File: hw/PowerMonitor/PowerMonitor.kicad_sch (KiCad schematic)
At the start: 43 parts, among them J1 Conn_01x02_Socket, J2 Conn_01x02_Socket, J3 Conn_01x02_Socket, J4 Conn_01x02_Socket, J5 Conn_01x02_Socket, K1 Relay_SPST-NC, U1 TPS54202DDC, U2 74LVC1G32, U3 74LVC1G32, U4 NE555D

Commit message: Rework powermon
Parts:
- removed C1: 10 µF, Capacitor_SMD:C_0603_1608Metric_Pad1.08x0.95mm_HandSolder, symbol #inventree:CL21A106KOQNNNE
- removed C2, C3: 0.1 µF, Capacitor_SMD:C_0603_1608Metric_Pad1.08x0.95mm_HandSolder, symbol #inventree:CL21B104KBCNNNC
- removed C5, C6: 22 µF, Capacitor_SMD:C_0603_1608Metric_Pad1.08x0.95mm_HandSolder, symbol #inventree:CL21X226MOYNNWE
- removed D1: PESD15VL1BA, Diode_SMD:D_SOD-323_HandSoldering, symbol Device:D_TVS
- removed JP1: SolderJumper_2_Open, Jumper:SolderJumper-2_P1.3mm_Open_RoundedPad1.0x1.5mm, symbol Jumper:SolderJumper_2_Open
- removed L1: L_Ferrite_Coupled_1423, Inductor_SMD:L_CommonModeChoke_TDK_ACM7060, symbol Device:L_Ferrite_Coupled_1423
- removed L2: KOHER_MDA7030 15uH, Inductor_SMD:L_KOHERelec_MDA7030, symbol Device:L_Ferrite
- removed R1: 0 ohm, Resistor_SMD:R_0603_1608Metric_Pad0.98x0.95mm_HandSolder, symbol #inventree:RC0603FR-070RL
- removed R2: 100 kohm, Resistor_SMD:R_0603_1608Metric_Pad0.98x0.95mm_HandSolder, symbol #inventree:RC0603FR-07100KL
- removed R3: 22 kohm, Resistor_SMD:R_0603_1608Metric_Pad0.98x0.95mm_HandSolder, symbol #inventree:RC0603FR-0722KL
- removed TP1, TP2, TP3, TP4: TestPoint_Flag, TestPoint:TestPoint_Pad_1.0x1.0mm, symbol Connector:TestPoint_Flag
- removed U1: TPS54202DDC, Package_TO_SOT_SMD:SOT-23-6_Handsoldering, symbol Regulator_Switching:TPS54202DDC
- removed U2, U3: 74LVC1G32, Package_TO_SOT_SMD:SOT-353_SC-70-5_Handsoldering, symbol 74xGxx:74LVC1G32
- added C10: 470u, Capacitor_THT:CP_Radial_D4.0mm_P1.50mm, symbol Device:C_Polarized
- added C11: 1u, Capacitor_SMD:C_0603_1608Metric_Pad1.08x0.95mm_HandSolder, symbol Device:C
- added D5: PESD15VL1BA, Diode_SMD:D_SOD-323_HandSoldering, symbol Device:D_TVS
- added JP2: SolderJumper_2_Open, Jumper:SolderJumper-2_P1.3mm_Open_RoundedPad1.0x1.5mm, symbol Jumper:SolderJumper_2_Open
- added L3: L_Ferrite_Coupled_1423, Inductor_SMD:L_CommonModeChoke_TDK_ACM7060, symbol Device:L_Ferrite_Coupled_1423
- added R1: 50k, Resistor_SMD:R_0603_1608Metric_Pad0.98x0.95mm_HandSolder, symbol Device:R
- C4, C7: value 1u -> 100n
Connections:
- net +10V: now also C7.2, C8.1, U4.8 (VCC), C10.1, C11.2, D5.2 (A2)
- net +3V3: no longer C4.1, C7.1, C8.1, U4.8 (VCC)
- net GND: now also BT3.2 (-), C4.1, C7.1, C8.2, C10.2, C11.1, D5.1 (A1), R1.2
- net GNDREF: no longer BT3.2 (-), C4.2, C7.2, C8.2
- net CellMonitor1/UVOV: now reaches U4.2 (TR)
- net CellMonitor1/UVOV: now also C4.2, R1.1
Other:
- sheet CellMonitor1 ports: added UVOV; removed UVLO
- sheet CellMonitor2 ports: added UVOV; removed UVLO
- sheet CellMonitor3 ports: added UVOV; removed UVLO
- moved on the sheet: BT1, BT2, BT3, C22, C8, C9, D8, D9, J1, J2, J3, J4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

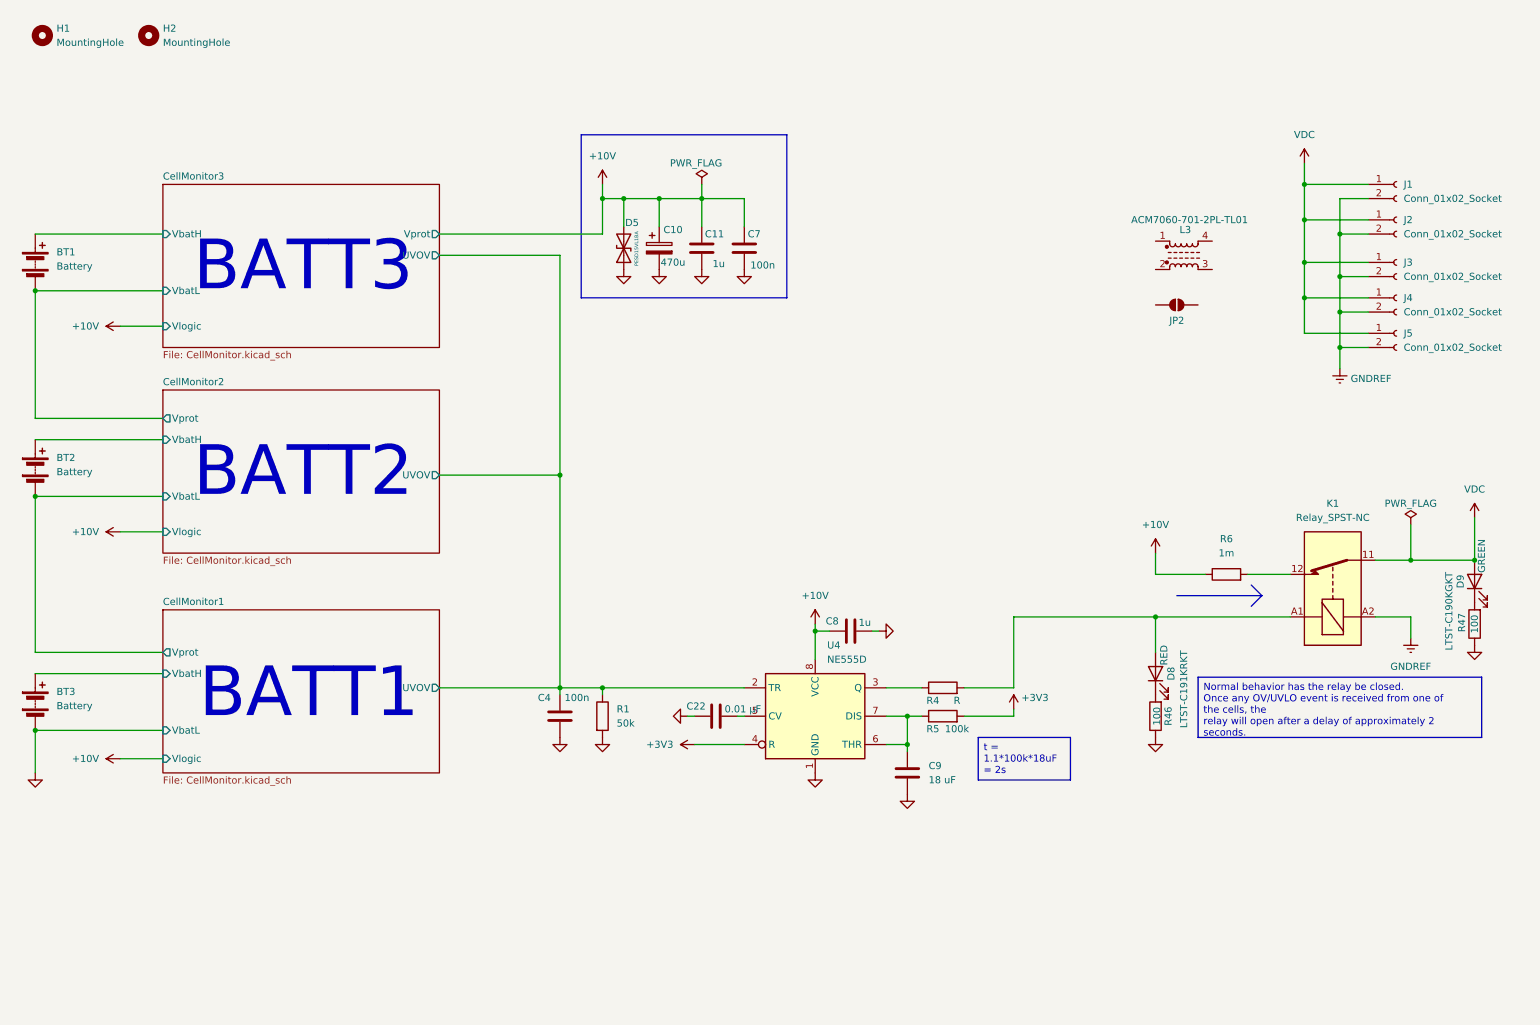
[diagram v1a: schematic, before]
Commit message: ad uvov in powermon, overcurrent and prepare for latch alarm
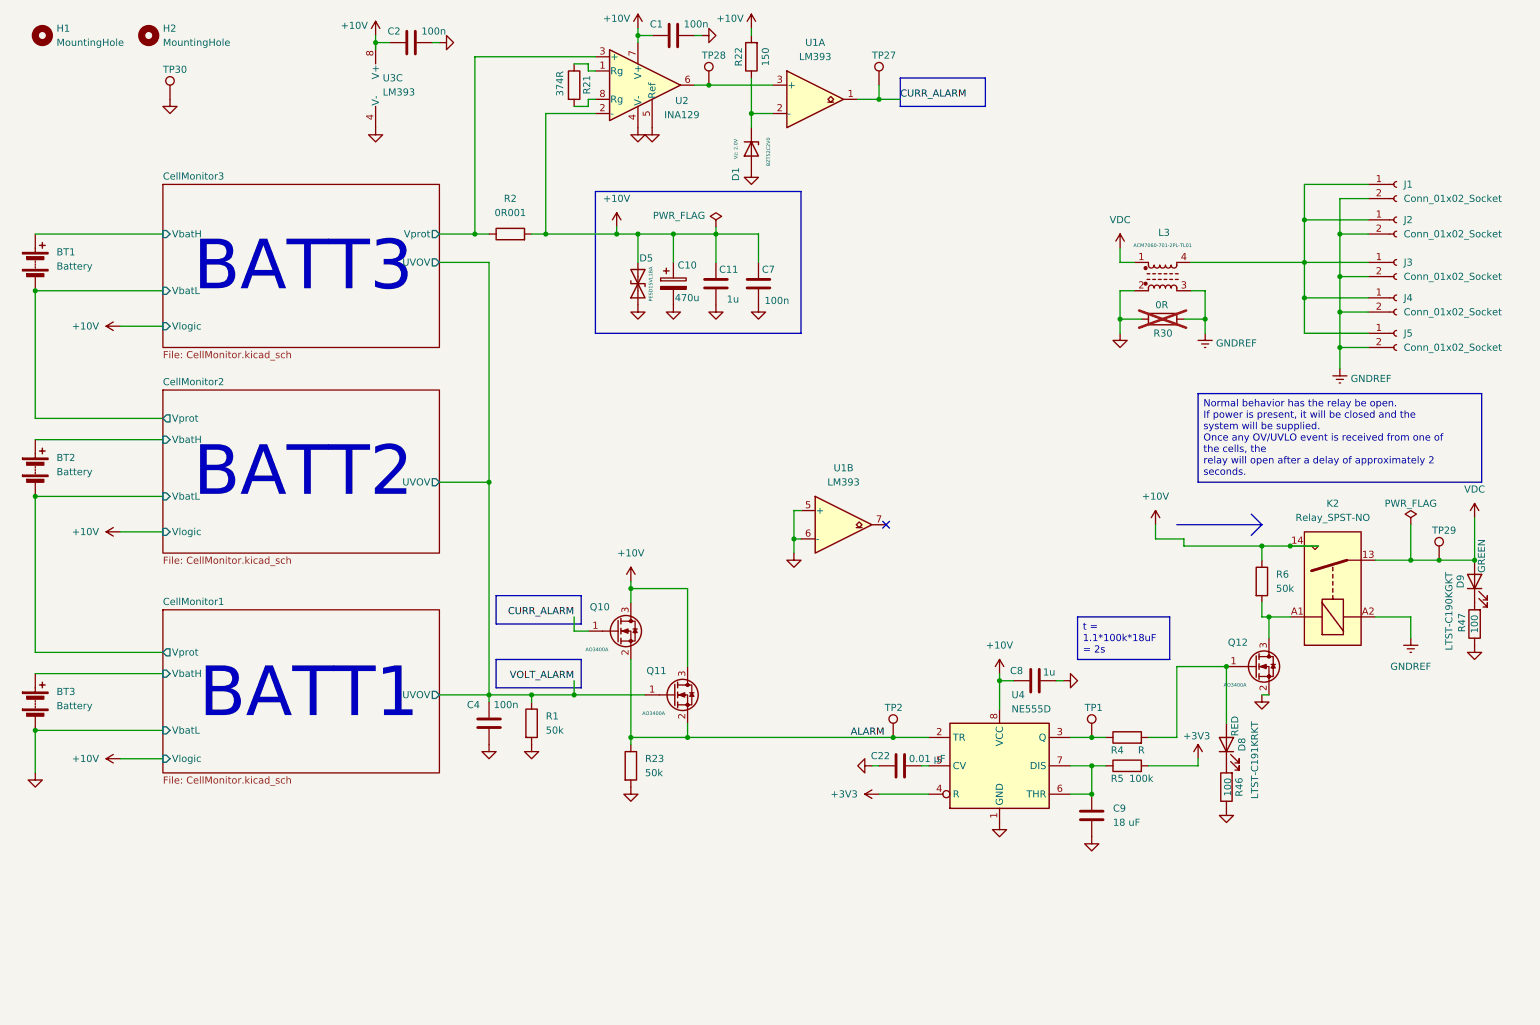
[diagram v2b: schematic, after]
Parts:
- removed JP2: SolderJumper_2_Open, Jumper:SolderJumper-2_P1.3mm_Open_RoundedPad1.0x1.5mm, symbol Jumper:SolderJumper_2_Open
- removed K1: Relay_SPST-NC, symbol Relay:Relay_SPST-NC
- added C1, C2: 100n, Capacitor_SMD:C_0603_1608Metric_Pad1.08x0.95mm_HandSolder, symbol Device:C
- added D1: BZT52Bxx, Diode_SMD:D_SOD-123F, symbol Diode:BZT52Bxx
- added K2: Relay_SPST-NO, symbol Relay:Relay_SPST-NO
- added Q10, Q11, Q12: AO3400A, Package_TO_SOT_SMD:SOT-23_Handsoldering, symbol Transistor_FET:AO3400A
- added R2: 0R001, Resistor_SMD:R_2512_6332Metric_Pad1.40x3.35mm_HandSolder, symbol Device:R
- added R21: 374R, Resistor_SMD:R_0603_1608Metric_Pad0.98x0.95mm_HandSolder, symbol Device:R
- added R22: 150, Resistor_SMD:R_0603_1608Metric_Pad0.98x0.95mm_HandSolder, symbol Device:R
- added R23: 50k, Resistor_SMD:R_0603_1608Metric_Pad0.98x0.95mm_HandSolder, symbol Device:R
- added R30: 0R, Resistor_SMD:R_0603_1608Metric_Pad0.98x0.95mm_HandSolder, symbol Device:R
- added TP1, TP2, TP27, TP28, TP29, TP30: TestPoint, Connector_Pin:Pin_D1.4mm_L8.5mm_W2.8mm_FlatFork, symbol Connector:TestPoint
- added U1, U3: LM393, Package_SO:SOIC-8_3.9x4.9mm_P1.27mm, symbol Comparator:LM393
- added U2: INA129, Package_SO:SOIC-8_5.3x6.2mm_P1.27mm, symbol Amplifier_Instrumentation:INA129
- R6: value 1m -> 50k; footprint Resistor_SMD:R_2512_6332Metric_Pad1.40x3.35mm_HandSolder -> Resistor_SMD:R_0603_1608Metric_Pad0.98x0.95mm_HandSolder
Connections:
- net +10V: now also C1.2, C2.2, K2.14, Q10.3 (D), Q11.3 (D), R2.2, R22.2, U2.2 (-), U2.7 (V+), U3.8 (V+)
- net GND: now also L3.2, C1.1, C2.1, D1.2 (A), Q12.2 (S), R23.2, R30.2, TP30.1, U1.5 (+), U1.6 (-), U2.4 (V-), U2.5 (Ref), U3.4 (V-)
- net GNDREF: now also L3.3, K2.A2, R30.1
- net VDC: now also L3.1, K2.13, TP29.1; no longer J1.1 (Pin_1), J2.1 (Pin_1), J3.1 (Pin_1), J4.1 (Pin_1), J5.1 (Pin_1)
- net at R4.1, U4.3 (Q): now also TP1.1
- net at D8.2 (A), R4.2: now also Q12.1 (G)
- net at R6.2: now also K2.A1, Q12.3 (D)
- net at L3.4: now also J1.1 (Pin_1), J2.1 (Pin_1), J3.1 (Pin_1), J4.1 (Pin_1), J5.1 (Pin_1)
- net CellMonitor1/UVOV renamed VOLT_ALARM
- net VOLT_ALARM: now also Q11.1 (G); no longer U4.2 (TR)
- new net: R21.1, U2.1 (Rg)
- new net: R21.2, U2.8 (Rg)
- new net: D1.1 (K), R22.1, U1.2 (-)
- new net: TP28.1, U1.3 (+), U2.6
- new net ALARM: Q10.2 (S), Q11.2 (S), R23.1, TP2.1, U4.2 (TR)
- new net CURR_ALARM: Q10.1 (G), TP27.1, U1.1
- new net CellMonitor3/Vprot: R2.1, U2.3 (+)
- no-connect marks 0 -> 1
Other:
- moved on the sheet: C10, C11, C22, C4, C7, C8, C9, D5, D8, L3, R1, R4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

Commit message: * hw/PowerMonitor/CellMonitor.kicad_sch: start PCB layout
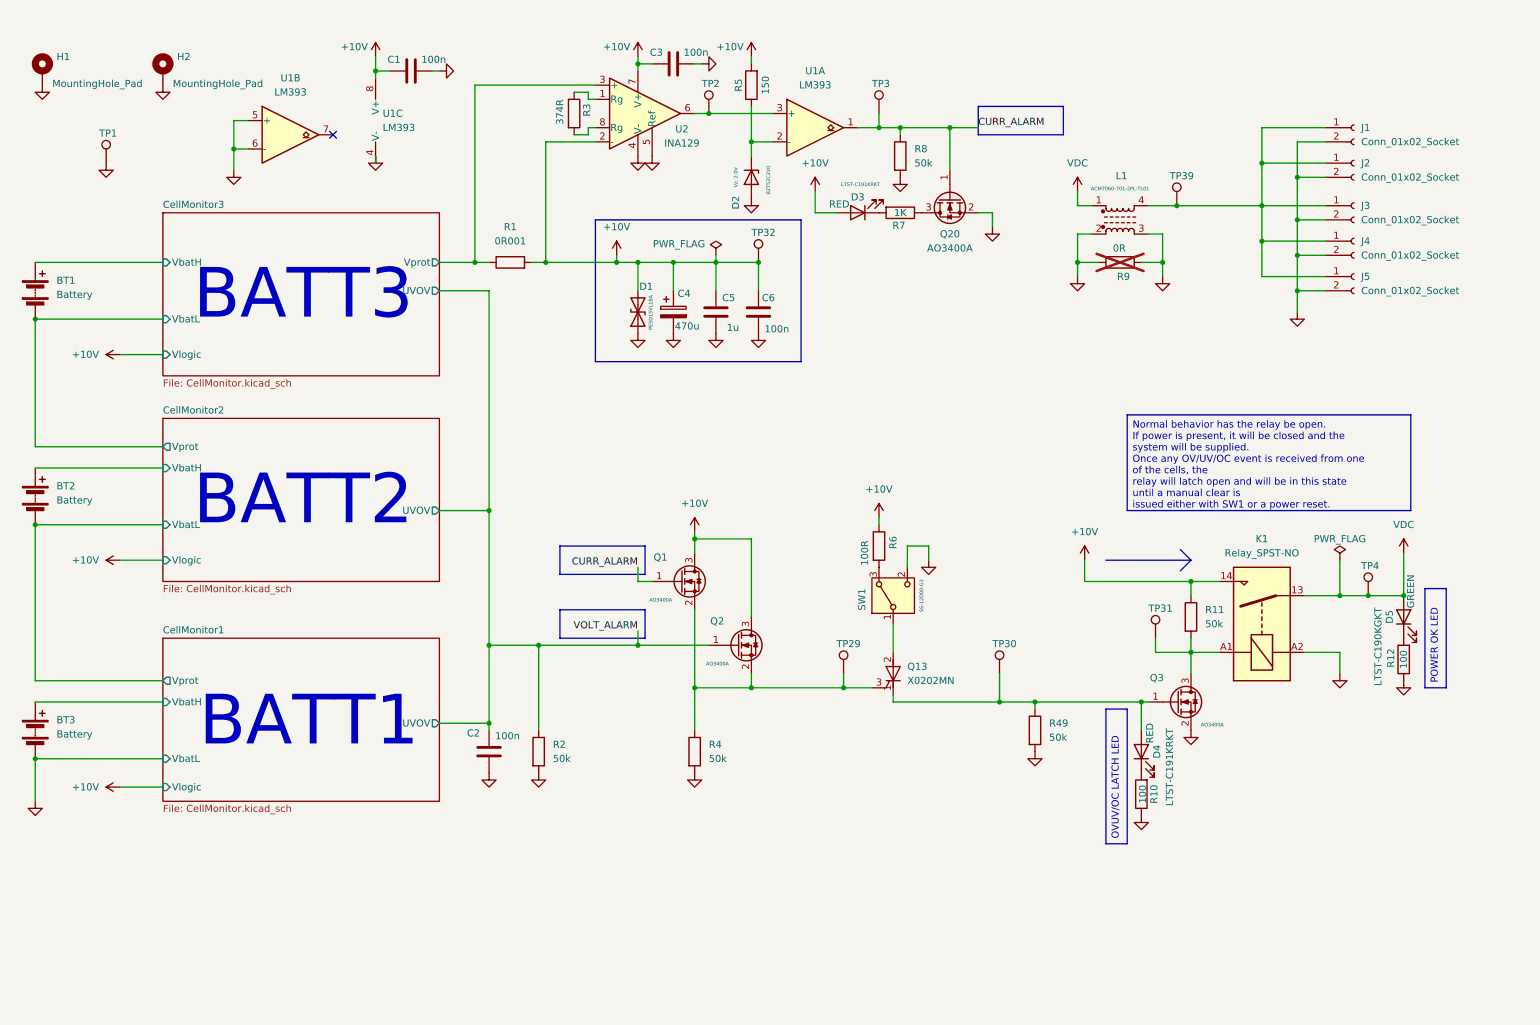
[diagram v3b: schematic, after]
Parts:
- removed C22: 0.01 µF, Capacitor_SMD:C_0603_1608Metric_Pad1.08x0.95mm_HandSolder, symbol #inventree:CL21B104KBCNNNC
- removed C8: 1u, Capacitor_SMD:C_0603_1608Metric_Pad1.08x0.95mm_HandSolder, symbol Device:C
- removed C9: 18 uF, Capacitor_SMD:C_0603_1608Metric_Pad1.08x0.95mm_HandSolder, symbol Device:C
- removed H1, H2: MountingHole, MountingHole:MountingHole_2.2mm_M2, symbol Mechanical:MountingHole
- removed R4: R, Resistor_SMD:R_0603_1608Metric_Pad0.98x0.95mm_HandSolder, symbol Device:R
- removed R5: 100k, Resistor_SMD:R_0603_1608Metric_Pad0.98x0.95mm_HandSolder, symbol Device:R
- removed TP1, TP2: TestPoint, Connector_Pin:Pin_D1.4mm_L8.5mm_W2.8mm_FlatFork, symbol Connector:TestPoint
- removed U4: NE555D, Package_SO:SOIC-8_3.9x4.9mm_P1.27mm, symbol Timer:NE555D
- added D3: RED, LED_SMD:LED_0603_1608Metric, symbol Device:LED
- added H1, H2: MountingHole_Pad, MountingHole:MountingHole_2.2mm_M2_Pad, symbol Mechanical:MountingHole_Pad
- added Q13: X0202MN, Package_TO_SOT_SMD:SOT-223, symbol Triac_Thyristor:X0202MN
- added Q20: AO3400A, Package_TO_SOT_SMD:SOT-23_Handsoldering, symbol Transistor_FET:AO3400A
- added R49, R8: 50k, Resistor_SMD:R_0603_1608Metric_Pad0.98x0.95mm_HandSolder, symbol Device:R
- added R6: 100R, Resistor_SMD:R_0603_1608Metric_Pad0.98x0.95mm_HandSolder, symbol Device:R
- added R7: 1K, Resistor_SMD:R_0603_1608Metric, symbol Device:R
- added SW1: SW_Wuerth_450301014042, Button_Switch_THT:SW_Slide-03_Wuerth-WS-SLTV_10x2.5x6.4_P2.54mm, symbol Switch:SW_Wuerth_450301014042
- added TP29, TP30, TP31, TP32, TP39: TestPoint, TestPoint:TestPoint_Pad_1.0x1.0mm, symbol Connector:TestPoint
- K1: renamed from K2; footprint (none) -> Relay_THT:Relay_SPST_Omron_G5NB; PN (none) -> G5NB-1A-E-24VDC
- TP1: renamed from TP30; footprint Connector_Pin:Pin_D1.4mm_L8.5mm_W2.8mm_FlatFork -> TestPoint:TestPoint_Pad_1.0x1.0mm
- TP2: renamed from TP28; footprint Connector_Pin:Pin_D1.4mm_L8.5mm_W2.8mm_FlatFork -> TestPoint:TestPoint_Pad_1.0x1.0mm
- TP3: renamed from TP27; footprint Connector_Pin:Pin_D1.4mm_L8.5mm_W2.8mm_FlatFork -> TestPoint:TestPoint_Pad_1.0x1.0mm
- TP4: renamed from TP29; footprint Connector_Pin:Pin_D1.4mm_L8.5mm_W2.8mm_FlatFork -> TestPoint:TestPoint_Pad_1.0x1.0mm
- renumbered C2 to C1, C4 to C2, C1 to C3, C10 to C4, C11 to C5, C7 to C6, D5 to D1, D1 to D2, D8 to D4, D9 to D5, L3 to L1, Q10 to Q1, Q11 to Q2, Q12 to Q3, R2 to R1, R46 to R10, R6 to R11, R47 to R12, R1 to R2, R21 to R3, R23 to R4, R22 to R5, R30 to R9, U3 to U1
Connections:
- net GNDREF is gone; now on net GND: J1.2 (Pin_2), J2.2 (Pin_2), J3.2 (Pin_2), J4.2 (Pin_2), J5.2 (Pin_2), K1.A2, L1.3, R9.1
- net +10V: now also D3.2 (A), R6.1, TP32.1
- net CURR_ALARM: now also Q20.1 (G), R8.1
- net GND: now also H1.1, H2.1, Q20.2 (S), R49.2, R8.2, SW1.2 (C)
- net at D4.2 (A), Q3.1 (G): now also Q13.1 (K), R49.1, TP30.1
- net at K1.A1, Q3.3 (D), R11.2: now also TP31.1
- net at J1.1 (Pin_1), J2.1 (Pin_1), J3.1 (Pin_1)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: now also TP39.1
- net ALARM: no longer names the net of Q1.2 (S), Q2.2 (S), R4.1
- net ALARM: now also Q13.3 (G), TP29.1
- new net: Q13.2 (A), Q13.4 (A), SW1.1 (B)
- new net: R6.2, SW1.3 (A)
- new net: Q20.3 (D), R7.1
- new net: D3.1 (K), R7.2
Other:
- moved on the sheet: BT1, BT2, BT3, C1, C2, C3, C4, C5, C6, D1, D2, D4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
